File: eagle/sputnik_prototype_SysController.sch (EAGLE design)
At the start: 70 parts, among them Q1 IRLML6344TRPBF, SW1 TPS25944LRVCRWQFN-20-3X4, U1 MEGA128-A, X1 CRYSTAL-ABRACON-ABM3-SMD

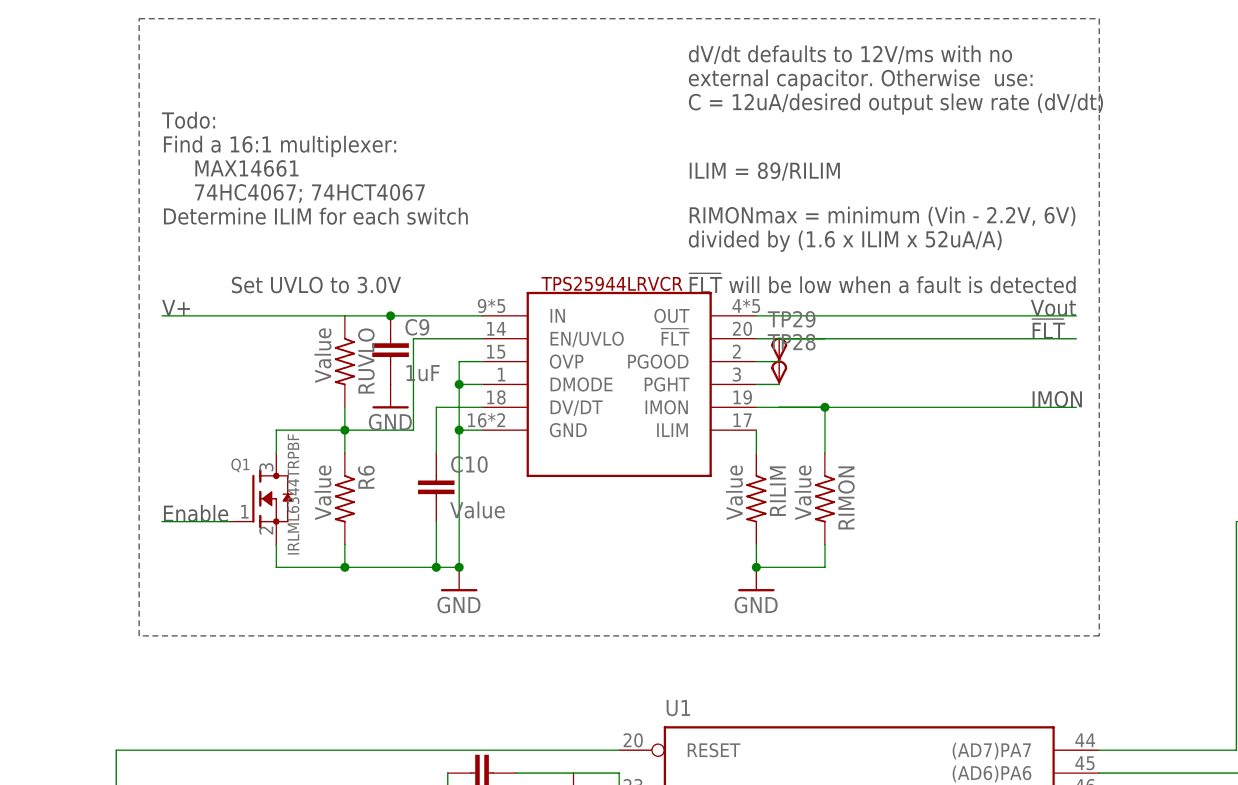
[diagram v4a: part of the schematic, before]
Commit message: added a pull up resistor to FLT
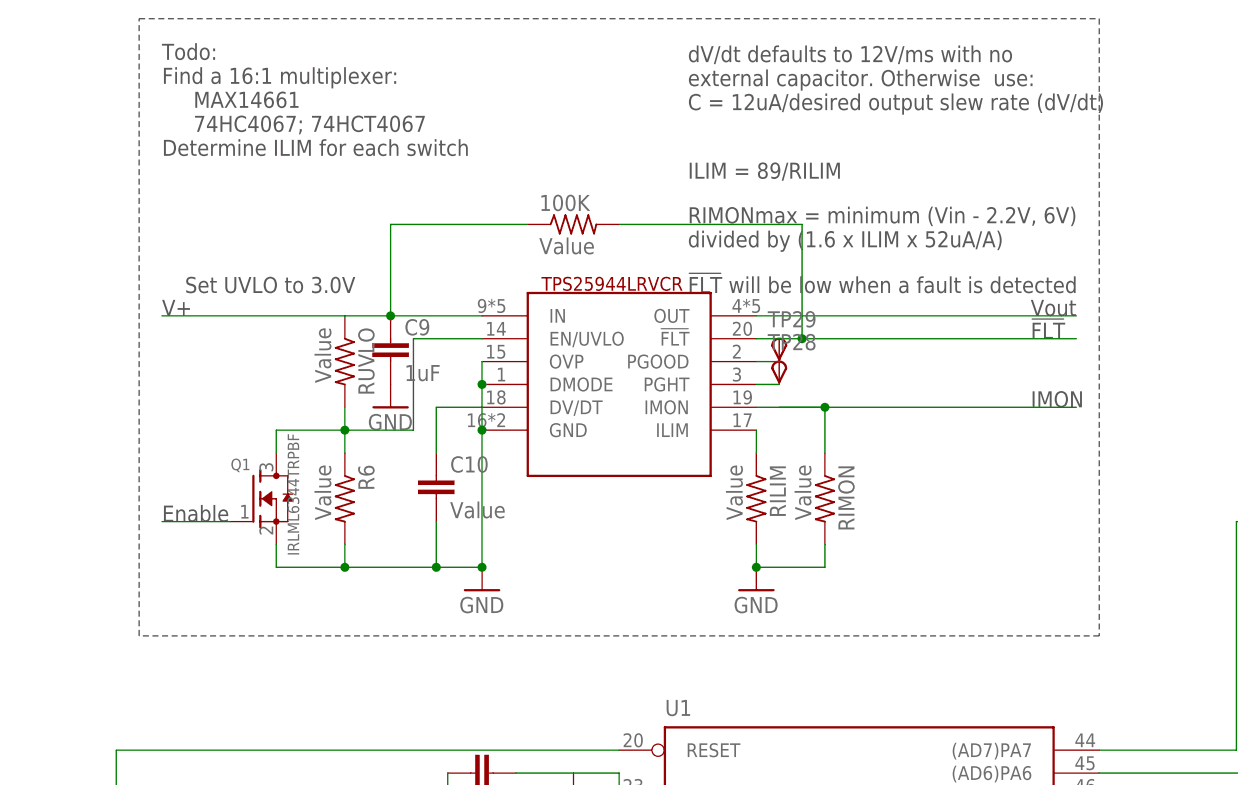
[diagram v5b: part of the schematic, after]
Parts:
- added 100K: Value, rcl_custom:R-US_0603-B-NOSILK
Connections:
- net N$2: now also 100K.1
- net N$29: now also 100K.2
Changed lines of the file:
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@@
 <part name="C10" library="rcl_custom" deviceset="C-EU" device="0402-B-NOSILK" value="Value"/>
 <part name="Q1" library="adafruit" deviceset="IRLML6344TRPBF" device=""/>
+<part name="100K" library="rcl_custom" deviceset="R-US_" device="0603-B-NOSILK" value="Value"/>
 </parts>
 <sheets>
@@
 8. ADS-Sunsensors
 9.ADS-Starfinder/Sunsensor</text>
-<text x="231.14" y="327.66" size="1.778" layer="97">Todo:
+<text x="231.14" y="335.28" size="1.778" layer="97">Todo:
 Find a 16:1 multiplexer:
      MAX14661
@@
 <wire x1="228.6" y1="281.94" x2="228.6" y2="350.52" width="0.1524" layer="97" style="longdash"/>
 <wire x1="228.6" y1="350.52" x2="335.28" y2="350.52" width="0.1524" layer="97" style="longdash"/>
-<text x="238.76" y="320.04" size="1.778" layer="97">Set UVLO to 3.0V</text>
+<text x="233.68" y="320.04" size="1.778" layer="97">Set UVLO to 3.0V</text>
 </plain>
 <instances>
@@
 </instance>
 <instance part="SW1" gate="G$1" x="281.94" y="309.88"/>
-<instance part="GND1" gate="1" x="264.16" y="287.02"/>
+<instance part="GND1" gate="1" x="266.7" y="287.02"/>
 <instance part="RUVLO" gate="R" x="251.46" y="312.42" smashed="yes" rot="R270">
 <attribute name="NAME" x="252.9586" y="316.23" size="1.778" layer="95" rot="R270"/>
@@
 <attribute name="NAME" x="238.76" y="300.355" size="1.27" layer="95"/>
 <attribute name="VALUE" x="246.38" y="290.83" size="1.27" layer="96" rot="R90"/>
+</instance>
+<instance part="100K" gate="R" x="276.86" y="327.66" smashed="yes">
+<attribute name="NAME" x="273.05" y="329.1586" size="1.778" layer="95"/>
+<attribute name="VALUE" x="273.05" y="324.358" size="1.778" layer="96"/>
 </instance>
 </instances>
@@
 <segment>
 <pinref part="SW1" gate="G$1" pin="GND"/>
-<wire x1="266.7" y1="304.8" x2="264.16" y2="304.8" width="0.1524" layer="91"/>
 <pinref part="SW1" gate="G$1" pin="DMODE"/>
-<wire x1="266.7" y1="309.88" x2="264.16" y2="309.88" width="0.1524" layer="91"/>
-<wire x1="264.16" y1="309.88" x2="264.16" y2="312.42" width="0.1524" layer="91"/>
 <pinref part="SW1" gate="G$1" pin="OVP"/>
-<wire x1="266.7" y1="312.42" x2="264.16" y2="312.42" width="0.1524" layer="91"/>
-<wire x1="264.16" y1="309.88" x2="264.16" y2="304.8" width="0.1524" layer="91"/>
-<wire x1="264.16" y1="304.8" x2="264.16" y2="289.56" width="0.1524" layer="91"/>
+<wire x1="266.7" y1="312.42" x2="266.7" y2="309.88" width="0.1524" layer="91"/>
+<wire x1="266.7" y1="309.88" x2="266.7" y2="304.8" width="0.1524" layer="91"/>
+<wire x1="266.7" y1="304.8" x2="266.7" y2="289.56" width="0.1524" layer="91"/>
 <pinref part="GND1" gate="1" pin="GND"/>
-<wire x1="261.62" y1="289.56" x2="264.16" y2="289.56" width="0.1524" layer="91"/>
-<junction x="264.16" y="304.8"/>
-<junction x="264.16" y="309.88"/>
-<junction x="264.16" y="289.56"/>
+<wire x1="261.62" y1="289.56" x2="266.7" y2="289.56" width="0.1524" layer="91"/>
+<junction x="266.7" y="304.8"/>
+<junction x="266.7" y="309.88"/>
+<junction x="266.7" y="289.56"/>
 <pinref part="C10" gate="CE" pin="2"/>
 <wire x1="261.62" y1="294.64" x2="261.62" y2="289.56" width="0.1524" layer="91"/>
@@
 <pinref part="C9" gate="CE" pin="1"/>
 <junction x="256.54" y="317.5"/>
+<wire x1="256.54" y1="317.5" x2="256.54" y2="327.66" width="0.1524" layer="91"/>
+<pinref part="100K" gate="R" pin="1"/>
+<wire x1="256.54" y1="327.66" x2="271.78" y2="327.66" width="0.1524" layer="91"/>
 </segment>
 </net>
@@
 <pinref part="SW1" gate="G$1" pin="OUT"/>
 <wire x1="297.18" y1="317.5" x2="332.74" y2="317.5" width="0.1524" layer="91"/>
-</segment>
-</net>
-<net name="N$7" class="0">
-<segment>
-<wire x1="299.72" y1="314.96" x2="332.74" y2="314.96" width="0.1524" layer="91"/>
 </segment>
 </net>
@@
 </segment>
 </net>
-<net name="N$29" class="0">
-<segment>
-<pinref part="SW1" gate="G$1" pin="!FLT"/>
-<wire x1="297.18" y1="314.96" x2="304.8" y2="314.96" width="0.1524" layer="91"/>
-</segment>
-</net>
 <net name="N$31" class="0">
 <segment>
@@
 </segment>
 </net>
+<net name="N$29" class="0">
+<segment>
+<pinref part="100K" gate="R" pin="2"/>
+<wire x1="281.94" y1="327.66" x2="302.26" y2="327.66" width="0.1524" layer="91"/>
+<wire x1="302.26" y1="327.66" x2="302.26" y2="314.96" width="0.1524" layer="91"/>
+<pinref part="SW1" gate="G$1" pin="!FLT"/>
+<wire x1="297.18" y1="314.96" x2="302.26" y2="314.96" width="0.1524" layer="91"/>
+<wire x1="302.26" y1="314.96" x2="332.74" y2="314.96" width="0.1524" layer="91"/>
+<junction x="302.26" y="314.96"/>
+</segment>
+</net>

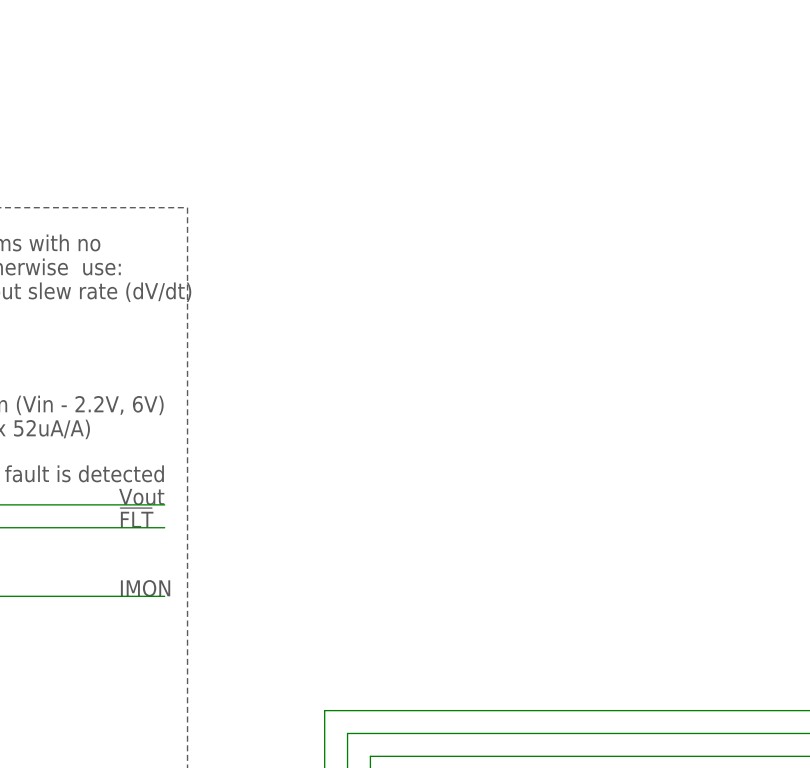
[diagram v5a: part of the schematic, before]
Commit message: added the mux to the schematic
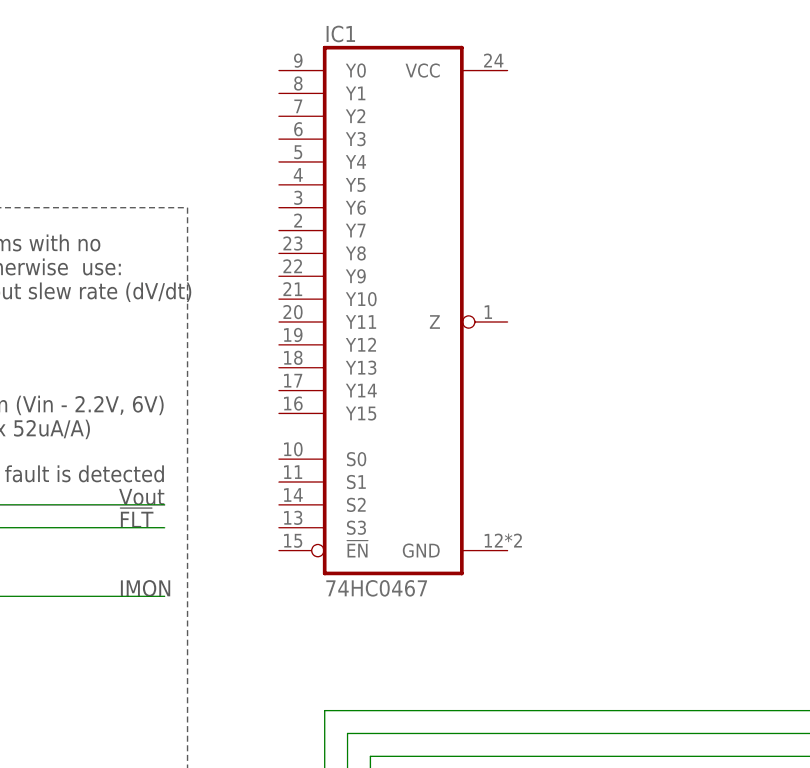
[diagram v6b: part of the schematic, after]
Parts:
- added IC1: 74HC0467, QFN-24:74HC0467
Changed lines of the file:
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@@
 <part name="Q1" library="adafruit" deviceset="IRLML6344TRPBF" device=""/>
 <part name="100K" library="rcl_custom" deviceset="R-US_" device="0603-B-NOSILK" value="Value"/>
+<part name="IC1" library="QFN-24" deviceset="74HC0467" device=""/>
 </parts>
 <sheets>
@@
 <attribute name="VALUE" x="273.05" y="324.358" size="1.778" layer="96"/>
 </instance>
+<instance part="IC1" gate="G$1" x="358.14" y="340.36"/>
 </instances>
 <busses>

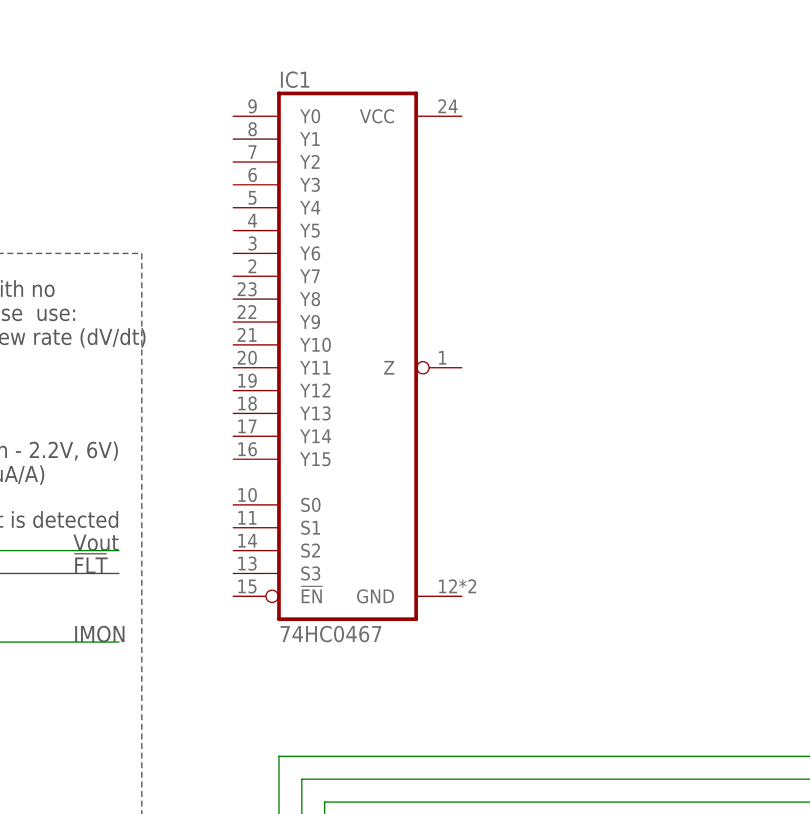
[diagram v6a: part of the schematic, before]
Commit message: added the updated mux to the schematic
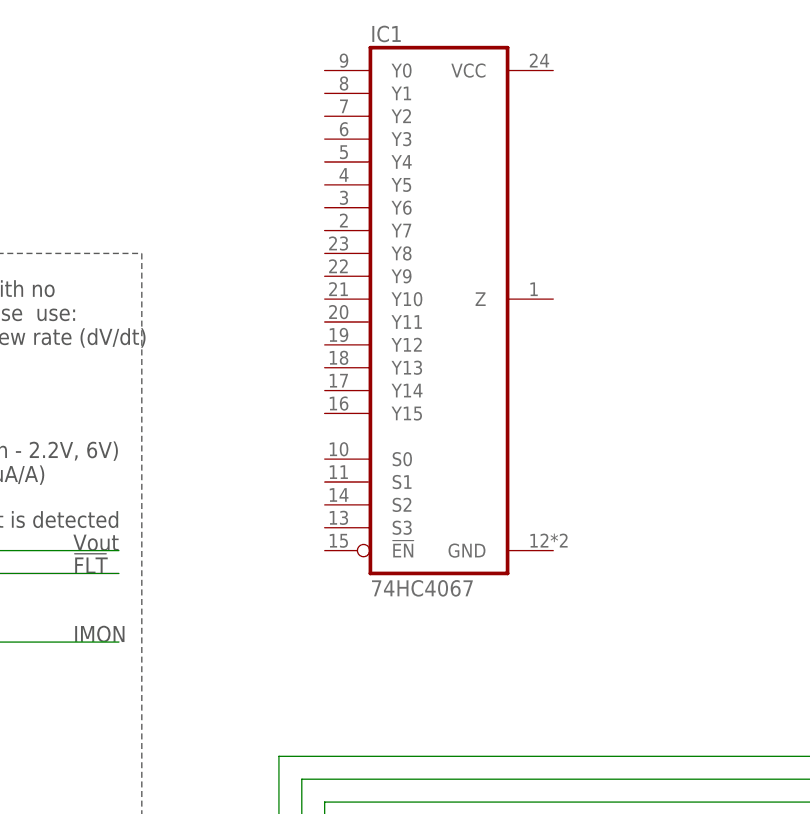
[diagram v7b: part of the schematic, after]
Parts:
- IC1: value 74HC0467 -> 74HC4067; device QFN-24:74HC0467 -> QFN-24:74HC4067
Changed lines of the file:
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@@
 <part name="Q1" library="adafruit" deviceset="IRLML6344TRPBF" device=""/>
 <part name="100K" library="rcl_custom" deviceset="R-US_" device="0603-B-NOSILK" value="Value"/>
-<part name="IC1" library="QFN-24" deviceset="74HC0467" device=""/>
+<part name="IC1" library="QFN-24" deviceset="74HC4067" device=""/>
 </parts>
 <sheets>
@@
 <attribute name="VALUE" x="273.05" y="324.358" size="1.778" layer="96"/>
 </instance>
-<instance part="IC1" gate="G$1" x="358.14" y="340.36"/>
+<instance part="IC1" gate="G$1" x="368.3" y="345.44"/>
 </instances>
 <busses>

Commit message: Added DNP LEDs and MOSFET drives to UARTs. Fixed TPS circuits with SOT-32-6 N/P MOSFET pair, which worked out nicely. Added another TPS to flesh it out, make sure it wasn't totally stupid. Added more DN LEDs to the outputs.
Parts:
- removed 100K: Value, rcl_custom:R-US_0603-B-NOSILK
- added C11: 1uF, rcl_custom:C-EU0603-B-NOSILK
- added C12: TBD, rcl_custom:C-EU0603-B-NOSILK
- added LED1, LED2: GRN, psas_c3_team05:LED-0603
- added LED3, LED4, LED5, LED6: DNP/AMB, psas_c3_team05:LED-0603
- added Q2: MOSFET-P-N-PAIR, ic-transistor-mosfet-n-p:MOSFET-P-N-PAIR
- added Q3, Q4, Q5, Q6: DNP/NTR4101P, Tova:NTR4101P
- added R13, R14, R17, R19, R20, R50: 47k, rcl_custom:R-US_0603-B-NOSILK
- added R15, R21: 1k, rcl_custom:R-US_0603-B-NOSILK
- added R16, RUVLO1: Value, rcl_custom:R-US_0603-B-NOSILK
- added R18, R9: 4.7k, rcl_custom:R-US_0603-B-NOSILK
- added R22, R23, R24, R25: DNP/1k, rcl_custom:R-US_0603-B-NOSILK
- added R4: 390, rcl_custom:R-US_0603-B-NOSILK
- added RILIM1, RIMON1: TBD, rcl_custom:R-US_0603-B-NOSILK
- added SW2: TPS25944LRVCRWQFN-20-3X4, WQFN-20-3x4:TPS25944LRVCRWQFN-20-3X4
- added TP30, TP4, TP5: TPSPAD1-13, testpad:TPSPAD1-13
- C10: value Value -> TBD; device rcl_custom:C-EU0402-B-NOSILK -> rcl_custom:C-EU0603-B-NOSILK
- C4, C40, C41, C9: device rcl_custom:C-EU0402-B-NOSILK -> rcl_custom:C-EU0603-B-NOSILK
- Q1: value IRLML6344TRPBF -> MOSFET-P-N-PAIR; device adafruit:IRLML6344TRPBF -> ic-transistor-mosfet-n-p:MOSFET-P-N-PAIR
- RILIM, RIMON: value Value -> TBD
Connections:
- net N$19 renamed RXD1
- net SDL renamed SCL
- removed net +3V3: C2.2, C3.2, C36.2, C37.2, C38.2, C39.2, C4.1, JP3.4, JP3.7, U$2.VDD, U$4.VDD, U$8.VOUT, U1.AREF, U1.AVCC, U1.VCC, U1.VCC@1
- removed net N$10: R3.2, U1.(TXD1/INT3)PD3
- removed net PA0: TP6.PP, U1.(AD0)PA0
- removed net PA1: TP3.PP, U1.(AD1)PA1
- removed net PC0: TP27.PP, U1.(A8)PC0
- removed net PC1: TP26.PP, U1.(A9)PC1
- removed net PTA1: R7.2, U1.(TXD/PDO)PE1
- removed net PTA2: R8.2, U1.(RXD/PDI)PE0
- new net 3V: C2.2, C3.2, C36.2, C37.2, C38.2, C39.2, C4.1, JP3.4, JP3.7, Q3.S, Q4.S, Q5.S, Q6.S, R17.1, R4.1, R50.1, U$2.VDD, U$4.VDD, U$8.VOUT, U1.AREF, U1.AVCC, U1.VCC, U1.VCC@1
- new net ILIM_ANALOG_IN: U1.PF0(ADC0)
- new net N$30: RILIM1.1, SW2.ILIM
- new net N$32: SW2.PGOOD, TP30.PP
- new net N$33: TP4.PP, U1.PEN
- new net N$34: U1.PF3(ADC3)
- new net N$35: U1.PF2(ADC2)
- new net N$37: U1.PF1(ADC1)
- new net N$38: C12.1, SW2.DV/DT
- new net N$39: U1.(XCK0/AIN0)PE2
- new net N$40: U1.(OC3A/AIN1)PE3
- new net N$41: U1.(OC3B/INT4)PE4
- new net N$42: U1.(OC3C/INT5)PE5
- new net N$43: U1.(T3/INT6)PE6
- new net N$44: U1.(IC3/INT7)PE7
- new net N$45: U1.(IC1)PD4
- new net N$46: U1.(XCK1)PD5
- new net N$47: U1.(T1)PD6
- new net N$48: U1.(T2)PD7
- new net N$49: Q1A.G, R18.2, R19.2
- new net N$50: Q1B.D, RUVLO1.1
- new net N$51: Q1A.D, Q1B.G, R20.1
- new net N$52: LED2.A, R21.2
- new net N$53: LED3.A, R22.2
- new net N$54: Q3.D, R22.1
- new net N$55: LED4.A, R23.2
- new net N$56: Q4.D, R23.1
- new net N$57: LED5.A, R24.2
- new net N$58: Q5.D, R24.1
- new net N$60: LED6.A, R25.2
- new net N$61: Q6.D, R25.1
- new net N$7: Q2A.D, Q2B.G, R14.1
- new net NUCLEAROPTION0: U1.PG0(WR)
- new net NUCLEAROPTION1: U1.PG1(RD)
- new net NUCLEAROPTION2: U1.PG2(ALE)
- new net RXD0: Q3.G, R8.2, U1.(RXD/PDI)PE0
- new net TXD0: Q4.G, R7.2, U1.(TXD/PDO)PE1
- new net TXD1: Q6.G, R3.2, U1.(TXD1/INT3)PD3
- new net VCB0: CF2.1, CF2.2, CF2.3, CF2.4, R15.1, SW1.OUT
- new net VCB0_!FLT: R50.2, SW1.!FLT, TP27.PP, U1.(A8)PC0
- new net VCB0_EN: R9.1, TP6.PP, U1.(AD0)PA0
- new net VCB0_IMON: IC1.Y0, RIMON.1, SW1.IMON
- new net VCB1: CF2.6, CF2.7, CF2.8, CF2.9, R21.1, SW2.OUT
- new net VCB1_!FLT: R17.2, SW2.!FLT, TP26.PP, U1.(A9)PC1
- new net VCB1_EN: R18.1, TP3.PP, U1.(AD1)PA1
- new net VCB1_IMON: RIMON1.1, SW2.IMON
- new net VCB2: CF2.11, CF2.12, CF2.13, CF2.14
- new net VCB3: CF2.16, CF2.17, CF2.18, CF2.19
- net GND: now also C11.2, C12.2, CF2.10, CF2.15, CF2.5, LED1.K, LED2.K, LED3.K, LED4.K, LED5.K, LED6.K, Q1A.S, Q2A.S, R13.1, R16.2, R19.1, RILIM1.2, RIMON1.2, SW1.PGHT, SW2.DMODE, SW2.GND, SW2.OVP, SW2.PGHT, TP28.PP, TP5.PP, U$2.GND1; no longer Q1.S
- net N$15: now also R4.2
- net N$2: now also Q2A.G, R13.2, R9.2; no longer 100K.1, C9.1, RUVLO.1, SW1.IN
- net N$26: now also LED1.A, R15.2; no longer Q1.G
- net N$27: now also U1.PG3(TOSC2); no longer RIMON.1, SW1.IMON
- net N$28: now also U1.PG4(TOSC1); no longer SW1.PGHT, TP28.PP
- net N$29: now also R16.1, RUVLO1.2, SW2.EN/UVLO; no longer 100K.2, SW1.!FLT
- net N$3: now also Q2B.D, RUVLO.1; no longer SW1.OUT
- net N$9: no longer Q1.D
- net VBUS: now also C11.1, C9.1, Q1B.S, Q2B.S, R14.2, R20.2, SW1.IN, SW2.IN
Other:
- note added: "CHECK POLARITY"
- note added: "Power Control for: 1. LGR 2. FC 3. DxWiFi 4. ACS-RW 5. ACS-MAG 6. IMU 7. SDR-GPS"
- note added: "UART0 RX"
- note added: "UART0 TX"
- note added: "UART1 RX"
- note added: "UART1 TX"
- note removed: "!FLT"
- note removed: "Enable"
- note removed: "IMON"
- note removed: "Power Control for: 0. SPS/SBS (nuclear option) 1. LGR 2. FC 3. DxWiFi PA 4. ACS-RW 5. ACS-MAG 6. IMU 7. SDR-GPS 8. ADS-Sunsensors 9.ADS-Starfinder/Sunsensor"
- note removed: "Power interface"
- note removed: "V+"
- note removed: "Vout"
- moved on the sheet: C1, C10, C2, C3, C36, C37, C38, C39, C4, C40, C41, C5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
